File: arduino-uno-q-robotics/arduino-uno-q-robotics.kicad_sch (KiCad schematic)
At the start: 17 parts, among them J1 Conn_02x30_Odd_Even, J2 Conn_02x30_Odd_Even, J3 Connector_FFC-FPC, J4 Connector_FFC-FPC, J5 Conn_02x30_Odd_Even, U1 LSM6DSO32, U2 TCA9803, U4 TCA9803

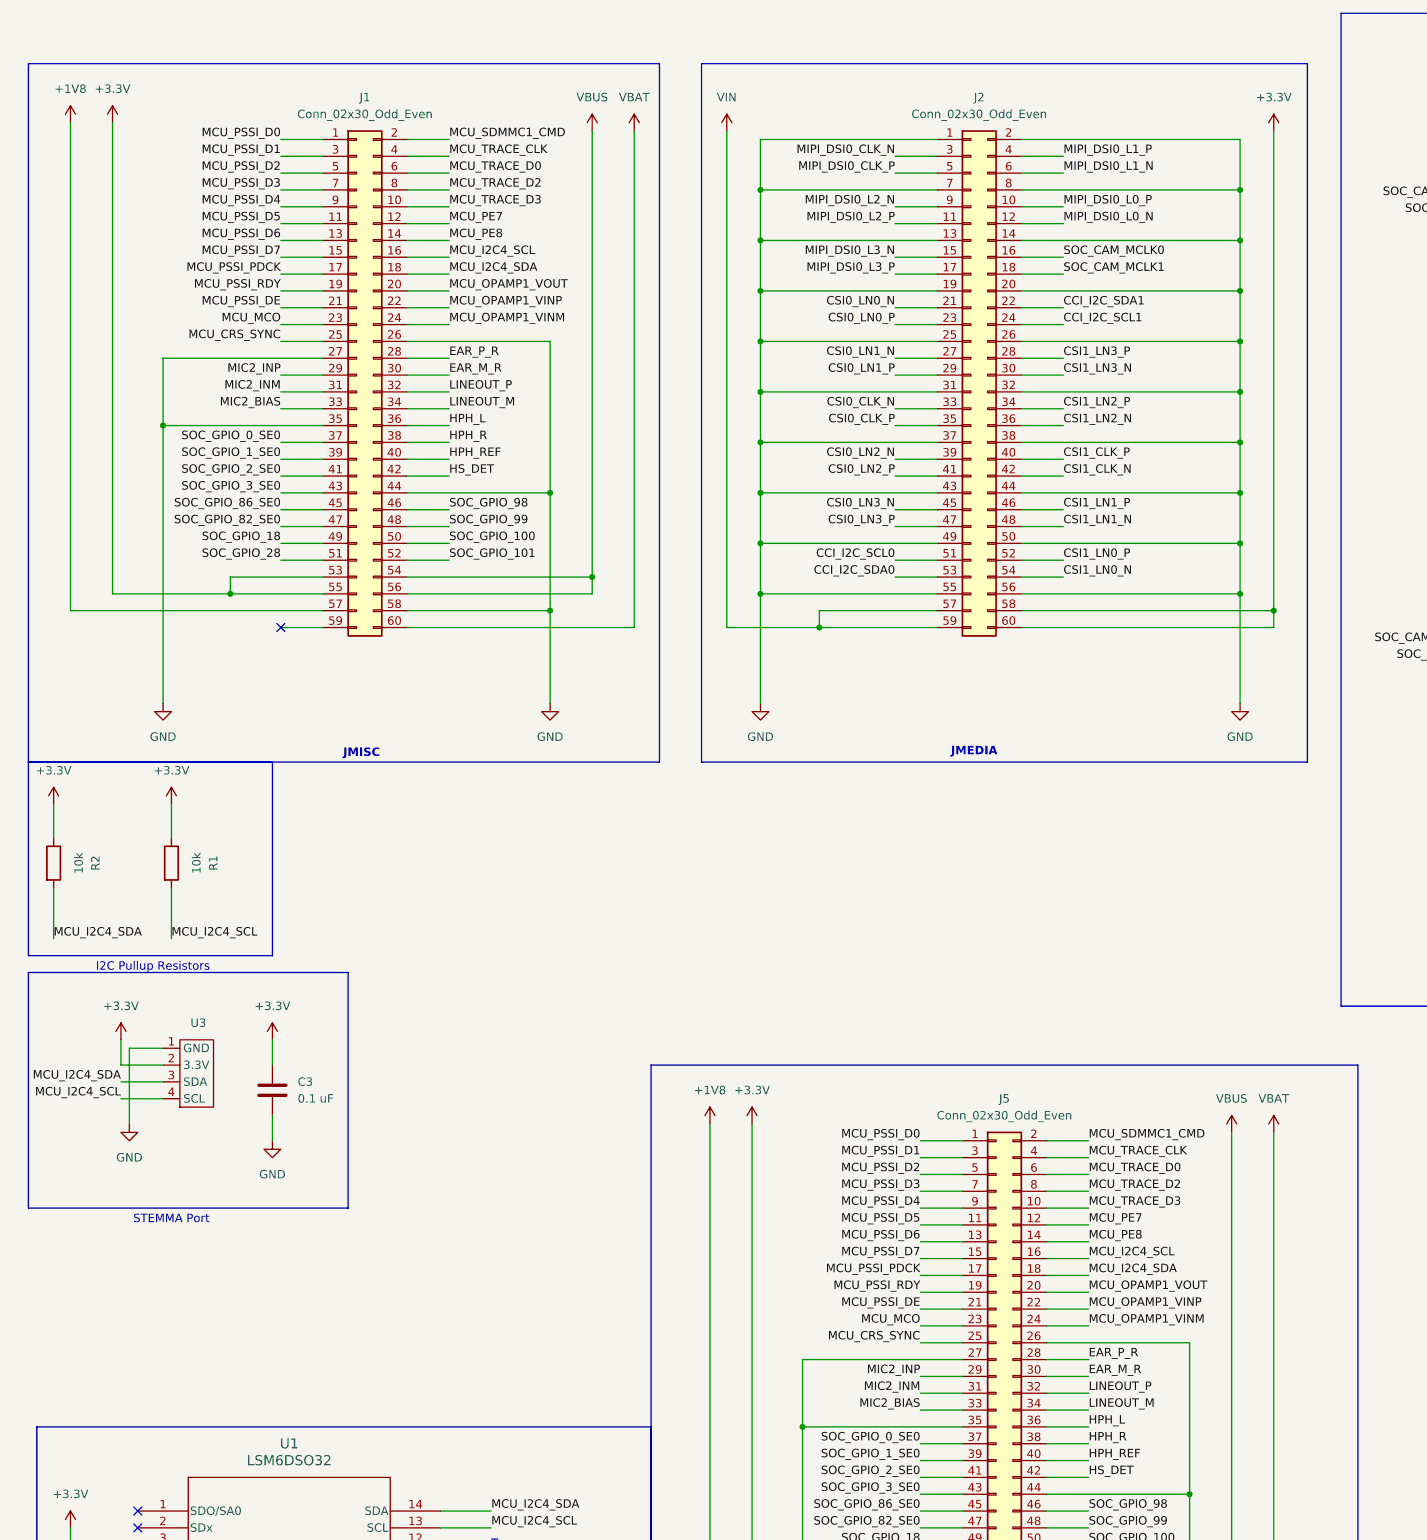
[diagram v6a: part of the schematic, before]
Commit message: Reconnect MCLK0 to camera connector
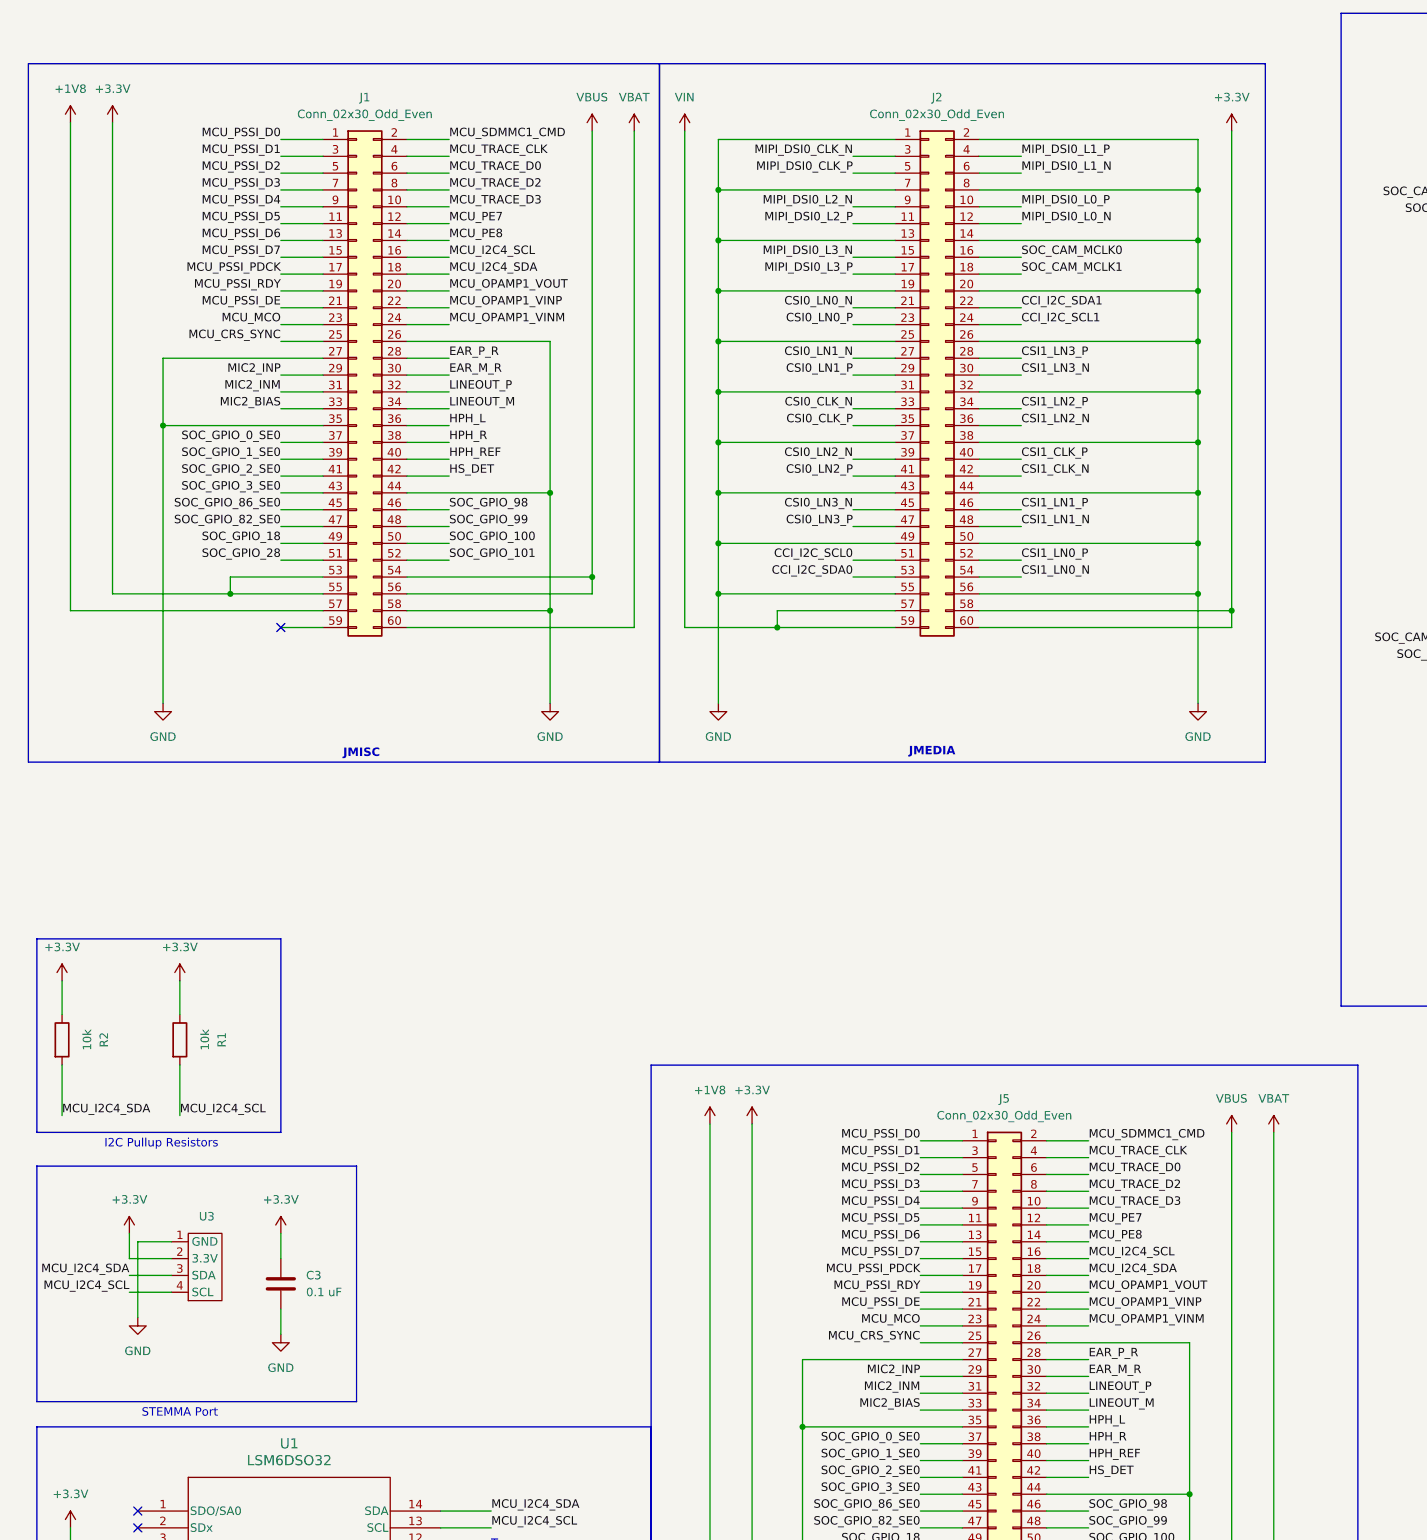
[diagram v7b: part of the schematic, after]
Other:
- moved on the sheet: C3, J2, R1, R2, U3

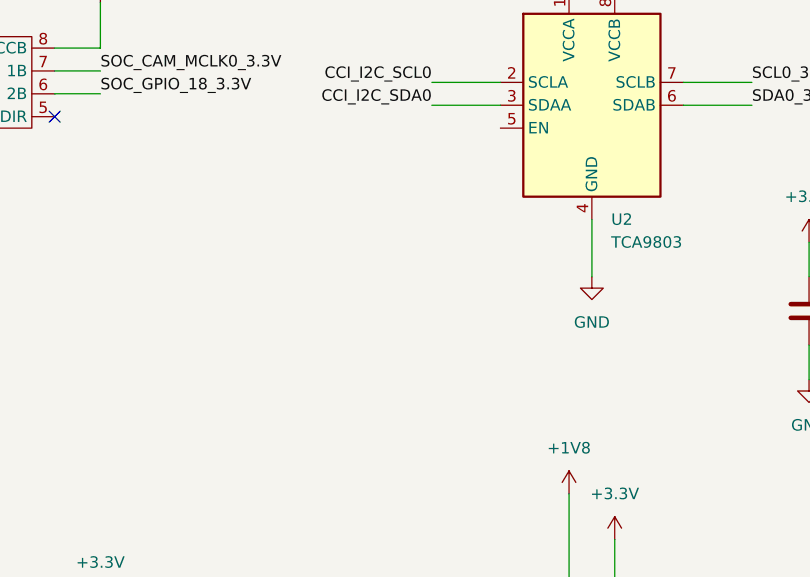
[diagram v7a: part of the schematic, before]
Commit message: Adjust placement of decoups and pullup resistors
Update arduino-uno-q-robotics.kicad_sch
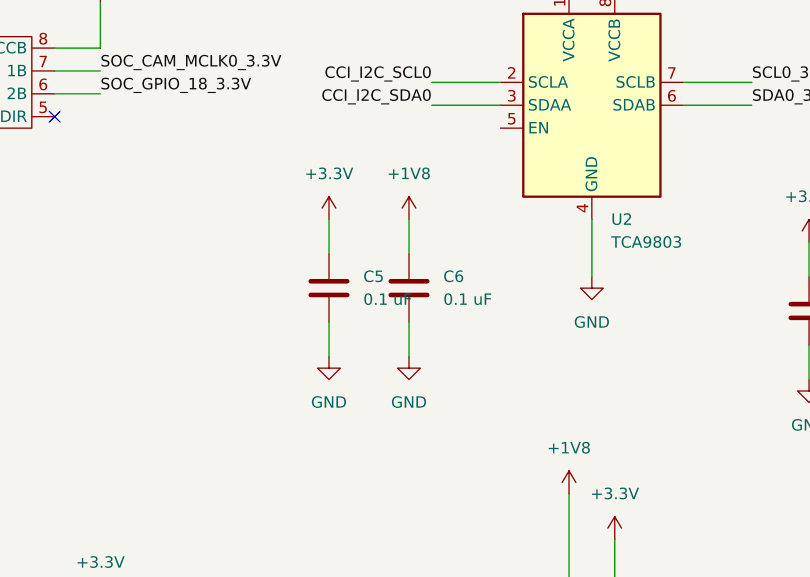
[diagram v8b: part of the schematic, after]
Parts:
- added C5, C6: 0.1 uF, Capacitor_SMD:C_0603_1608Metric_Pad1.08x0.95mm_HandSolder, symbol Device:C
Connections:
- net +1V8: now also C6.1
- net +3.3V: now also C5.1
- net GND: now also C5.2, C6.2
